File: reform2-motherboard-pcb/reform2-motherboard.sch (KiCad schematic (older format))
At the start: 44 parts, among them J15 Conn_01x33, J18 Conn_01x03_Male, J19 JTAG, J20 Conn_01x03_Male, SW3 SW_DIP_x01, SW5 SW_DIP_x04, SW6 SW_Push, U1 Nitrogen8M

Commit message: reform2-motherboard: schematics,PCB,BOM,models for R-2C (probably final)
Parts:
- H1, H2, H3: footprint MountingHole:MountingHole_3.2mm_M3_DIN965_Pad -> footprints:WA-SMSI-M2
- J19: footprint Connector_PinHeader_2.54mm:PinHeader_2x04_P2.54mm_Vertical -> Connector_PinHeader_1.27mm:PinHeader_2x05_P1.27mm_Vertical; symbol Connector:Conn_01x08_Male -> Connector:Conn_ARM_JTAG_SWD_10; Manufacturer_No 79425-408HLF -> 20021111-00010T4LF
- SW5: footprint Button_Switch_SMD:SW_DIP_SPSTx04_Slide_Omron_A6S-410x_W8.9mm_P2.54mm -> Button_Switch_SMD:SW_DIP_SPSTx04_Slide_Copal_CHS-04B_W7.62mm_P1.27mm; Manufacturer Omron -> Diptronics; Manufacturer_No A6S-4101-H -> DHA-04TQ
- SW6: footprint Button_Switch_SMD:SW_Push_1P1T_NO_CK_KMR2 -> footprints:UK-B0206-G3.8-250-JZ; Manufacturer C&K -> USAKRO; Manufacturer_No KMR221GLFS -> UK-B0206-G3.8-250-JZ
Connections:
- net ETH0_LED_LINK2: now also J19.10 (~RESET~); no longer J19.7 (Pin_7)
- net GND: now also J19.3 (GND), J19.9 (GNDDetect); no longer J19.8 (Pin_8)
- net IMX_JTAG_TDI: now also J19.8 (NC/TDI); no longer J19.2 (Pin_2)
- net IMX_JTAG_TMS: now also J19.2 (SWDIO/TMS); no longer J19.3 (Pin_3)
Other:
- moved on the sheet: R120
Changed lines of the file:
@@
 Sheet 1 9
 Title "MNT Reform 2"
-Date "2020-09-24"
-Rev "2.0R-1"
+Date "2020-10-29"
+Rev "2.0R-2C"
 Comp "MNT Research GmbH"
 Comment1 "https://mntre.com"
@@
 Text GLabel 6600 5350 0    50   Output ~ 0
 PCIE1_RESETn
-Text Notes 15250 4750 0    50   ~ 0
+Text Notes 14850 4400 0    50   ~ 0
 NOSTUFF
-Text Notes 14850 4750 0    50   ~ 0
-NOSTUFF
-Text Notes 15600 4750 0    50   ~ 0
+Text Notes 15550 4400 0    50   ~ 0
 NOSTUFF
 Wire Wire Line
@@
 	1    0    0    -1
 $EndComp
-Connection ~ 15650 5650
-Wire Wire Line
-	15650 5650 14800 5650
-Wire Wire Line
-	15650 5650 16050 5650
-Wire Wire Line
-	15950 5950 15950 5750
 $Comp
 L power:GND #PWR0219
 U 1 1 5F0CE58E
-P 15950 5950
-F 0 "#PWR0219" H 15950 5700 50  0001 C CNN
-F 1 "GND" H 15955 5777 50  0000 C CNN
-F 2 "" H 15950 5950 50  0001 C CNN
-F 3 "" H 15950 5950 50  0001 C CNN
-	1    15950 5950
-	1    0    0    -1
-$EndComp
-Wire Wire Line
-	15950 4450 15650 4450
-Connection ~ 15950 4450
-Wire Wire Line
-	15050 6050 15050 6000
+P 16750 6350
+F 0 "#PWR0219" H 16750 6100 50  0001 C CNN
+F 1 "GND" H 16755 6177 50  0000 C CNN
+F 2 "" H 16750 6350 50  0001 C CNN
+F 3 "" H 16750 6350 50  0001 C CNN
+	1    16750 6350
+	1    0    0    -1
+$EndComp
+Wire Wire Line
+	16750 4450 15650 4450
+Connection ~ 16750 4450
+Wire Wire Line
+	15950 6000 15950 5950
 $Comp
 L power:GND #PWR0218
 U 1 1 5F0856B7
-P 15050 6050
-F 0 "#PWR0218" H 15050 5800 50  0001 C CNN
-F 1 "GND" H 15055 5877 50  0000 C CNN
-F 2 "" H 15050 6050 50  0001 C CNN
-F 3 "" H 15050 6050 50  0001 C CNN
-	1    15050 6050
+P 15950 6000
+F 0 "#PWR0218" H 15950 5750 50  0001 C CNN
+F 1 "GND" H 15955 5827 50  0000 C CNN
+F 2 "" H 15950 6000 50  0001 C CNN
+F 3 "" H 15950 6000 50  0001 C CNN
+	1    15950 6000
 	1    0    0    -1
 $EndComp
@@
 Wire Wire Line
 	15650 4450 15650 4500
-Wire Wire Line
-	16300 4450 15950 4450
 $Comp
 L power:+3V3 #PWR0103
 U 1 1 5F0466BE
-P 16300 4450
-F 0 "#PWR0103" H 16300 4300 50  0001 C CNN
-F 1 "+3V3" H 16315 4623 50  0000 C CNN
-F 2 "" H 16300 4450 50  0001 C CNN
-F 3 "" H 16300 4450 50  0001 C CNN
-	1    16300 4450
-	1    0    0    -1
-$EndComp
-Wire Wire Line
-	16050 5550 14800 5550
-Wire Wire Line
-	15050 5350 16050 5350
-Connection ~ 15050 5350
-Wire Wire Line
-	15050 5800 15050 5350
-Wire Wire Line
-	14800 5350 15050 5350
-Connection ~ 15050 5250
-Wire Wire Line
-	15050 5250 16050 5250
-Wire Wire Line
-	15050 5250 14800 5250
-Wire Wire Line
-	15050 4700 15050 5250
-Connection ~ 15350 5150
-Wire Wire Line
-	15350 5150 16050 5150
-Wire Wire Line
-	15350 5150 14800 5150
-Wire Wire Line
-	15350 4700 15350 5150
-Text GLabel 14800 5150 0    50   Input ~ 0
+P 16750 4450
+F 0 "#PWR0103" H 16750 4300 50  0001 C CNN
+F 1 "+3V3" H 16765 4623 50  0000 C CNN
+F 2 "" H 16750 4450 50  0001 C CNN
+F 3 "" H 16750 4450 50  0001 C CNN
+	1    16750 4450
+	1    0    0    -1
+$EndComp
+Wire Wire Line
+	16250 5500 14800 5500
+Wire Wire Line
+	15950 5750 15950 5300
+Wire Wire Line
+	15350 5600 14800 5600
+Text GLabel 14800 5600 0    50   Input ~ 0
 IMX_JTAG_TDI
-Text GLabel 14800 5250 0    50   Output ~ 0
+Text GLabel 14800 5400 0    50   Output ~ 0
 IMX_JTAG_TMS
 Text GLabel 8700 8350 0    50   Output ~ 0
@@
 F 0 "H3" H 16400 8699 50  0000 L CNN
 F 1 "NGFF-Mount3" H 16400 8608 50  0000 L CNN
-F 2 "MountingHole:MountingHole_3.2mm_M3_DIN965_Pad" H 16300 8650 50  0001 C CNN
+F 2 "footprints:WA-SMSI-M2" H 16300 8650 50  0001 C CNN
 F 3 "~" H 16300 8650 50  0001 C CNN
 F 4 "y" H 16300 8650 50  0001 C CNN "Checked"
@@
 F 0 "H2" H 16400 7999 50  0000 L CNN
 F 1 "NGFF-Mount2" H 16400 7908 50  0000 L CNN
-F 2 "MountingHole:MountingHole_3.2mm_M3_DIN965_Pad" H 16300 7950 50  0001 C CNN
+F 2 "footprints:WA-SMSI-M2" H 16300 7950 50  0001 C CNN
 F 3 "~" H 16300 7950 50  0001 C CNN
 F 4 "y" H 16300 7950 50  0001 C CNN "Checked"
@@
 F 0 "H1" H 16400 7349 50  0000 L CNN
 F 1 "NGFF-Mount1" H 16400 7258 50  0000 L CNN
-F 2 "MountingHole:MountingHole_3.2mm_M3_DIN965_Pad" H 16300 7300 50  0001 C CNN
+F 2 "footprints:WA-SMSI-M2" H 16300 7300 50  0001 C CNN
 F 3 "~" H 16300 7300 50  0001 C CNN
 F 4 "y" H 16300 7300 50  0001 C CNN "Checked"
@@
 L Device:R_Small R120
 U 1 1 5E4B7E2C
-P 15050 5900
-F 0 "R120" H 15109 5946 50  0000 L CNN
-F 1 "100k" H 15109 5855 50  0000 L CNN
-F 2 "Resistor_SMD:R_0603_1608Metric" H 15050 5900 50  0001 C CNN
-F 3 "~" H 15050 5900 50  0001 C CNN
-F 4 "Vishay Dale" H 15050 5900 50  0001 C CNN "Manufacturer"
-F 5 "CRCW0603100KJNEAC" H 15050 5900 50  0001 C CNN "Manufacturer_No"
-F 6 "y" H 15050 5900 50  0001 C CNN "Checked"
-F 7 "Mouser" H 15050 5900 50  0001 C CNN "Distributor"
-	1    15050 5900
+P 15950 5850
+F 0 "R120" H 16009 5896 50  0000 L CNN
+F 1 "100k" H 16009 5805 50  0000 L CNN
+F 2 "Resistor_SMD:R_0603_1608Metric" H 15950 5850 50  0001 C CNN
+F 3 "~" H 15950 5850 50  0001 C CNN
+F 4 "Vishay Dale" H 15950 5850 50  0001 C CNN "Manufacturer"
+F 5 "CRCW0603100KJNEAC" H 15950 5850 50  0001 C CNN "Manufacturer_No"
+F 6 "y" H 15950 5850 50  0001 C CNN "Checked"
+F 7 "Mouser" H 15950 5850 50  0001 C CNN "Distributor"
+	1    15950 5850
 	1    0    0    -1
 $EndComp
@@
 Text GLabel 7400 7750 0    50   Output ~ 0
 IMX_JTAG_TDO
-Text GLabel 14800 5650 0    50   Output ~ 0
+Text GLabel 14800 5100 0    50   Output ~ 0
 IMX_JTAG_RSTn
-Text GLabel 14800 5350 0    50   Output ~ 0
+Text GLabel 14800 5300 0    50   Output ~ 0
 IMX_JTAG_TCK
-Text GLabel 14800 5550 0    50   Output ~ 0
+Text GLabel 14800 5500 0    50   Output ~ 0
 IMX_JTAG_TDO
 $Comp
@@
 	1    18500 3200
 	0    1    1    0
-$EndComp
-$Comp
-L Switch:SW_Push SW?
-U 1 1 5DBC8BEC
-P 18750 3200
-AR Path="/5CC81028/5DBC8BEC" Ref="SW?"  Part="1"
-AR Path="/5DBC8BEC" Ref="SW6"  Part="1"
-F 0 "SW6" H 18750 3485 50  0000 C CNN
-F 1 "SW_Push" H 18750 3394 50  0000 C CNN
-F 2 "Button_Switch_SMD:SW_Push_1P1T_NO_CK_KMR2" H 18750 3400 50  0001 C CNN
-F 3 "~" H 18750 3400 50  0001 C CNN
-F 4 "C&K" H 18750 3200 50  0001 C CNN "Manufacturer"
-F 5 "KMR221GLFS" H 18750 3200 50  0001 C CNN "Manufacturer_No"
-F 6 "y" H 18750 3200 50  0001 C CNN "Checked"
-F 7 "Mouser" H 18750 3200 50  0001 C CNN "Distributor"
-	1    18750 3200
-	1    0    0    -1
 $EndComp
 Text GLabel 7500 8550 0    50   Output ~ 0
@@
 Text GLabel 7300 10750 0    50   Input ~ 0
 IMX_WAKE
-Wire Wire Line
-	15650 4700 15650 5650
-$Comp
-L Connector:Conn_01x08_Male J19
+$Comp
+L Connector:Conn_ARM_JTAG_SWD_10 J19
 U 1 1 5ECAAFCE
-P 16250 5350
-F 0 "J19" H 16222 5324 50  0000 R CNN
-F 1 "JTAG" H 16222 5233 50  0000 R CNN
-F 2 "Connector_PinHeader_2.54mm:PinHeader_2x04_P2.54mm_Vertical" H 16250 5350 50  0001 C CNN
-F 3 "~" H 16250 5350 50  0001 C CNN
-F 4 "Amphenol FCI" H 16250 5350 50  0001 C CNN "Manufacturer"
-F 5 "79425-408HLF" H 16250 5350 50  0001 C CNN "Manufacturer_No"
-F 6 "y" H 16250 5350 50  0001 C CNN "Checked"
-F 7 "Mouser" H 16250 5350 50  0001 C CNN "Distributor"
-	1    16250 5350
+P 16750 5400
+F 0 "J19" H 16500 6100 50  0000 R CNN
+F 1 "JTAG" H 16550 6000 50  0000 R CNN
+F 2 "Connector_PinHeader_1.27mm:PinHeader_2x05_P1.27mm_Vertical" H 16750 5400 50  0001 C CNN
+F 3 "~" H 16750 5400 50  0001 C CNN
+F 4 "Amphenol FCI" H 16750 5400 50  0001 C CNN "Manufacturer"
+F 5 "20021111-00010T4LF" H 16750 5400 50  0001 C CNN "Manufacturer_No"
+F 6 "y" H 16750 5400 50  0001 C CNN "Checked"
+F 7 "Mouser" H 16750 5400 50  0001 C CNN "Distributor"
+	1    16750 5400
 	-1   0    0    -1
 $EndComp
-Wire Wire Line
-	16050 5750 15950 5750
-Wire Wire Line
-	16050 5050 15950 5050
-Wire Wire Line
-	15950 4450 15950 5050
-Wire Wire Line
-	15950 5750 15950 5450
-Wire Wire Line
-	15950 5450 16050 5450
-Connection ~ 15950 5750
 $Comp
 L power:+5V #PWR0104
@@
 F 0 "SW5" H 18950 6017 50  0000 C CNN
 F 1 "SW_DIP_x04" H 18950 5926 50  0000 C CNN
-F 2 "Button_Switch_SMD:SW_DIP_SPSTx04_Slide_Omron_A6S-410x_W8.9mm_P2.54mm" H 18950 5550 50  0001 C CNN
-F 3 "~" H 18950 5550 50  0001 C CNN
-F 4 "Omron" H 18950 5550 50  0001 C CNN "Manufacturer"
-F 5 "A6S-4101-H" H 18950 5550 50  0001 C CNN "Manufacturer_No"
+F 2 "Button_Switch_SMD:SW_DIP_SPSTx04_Slide_Copal_CHS-04B_W7.62mm_P1.27mm" H 18950 5550 50  0001 C CNN
+F 3 "" H 18950 5550 50  0001 C CNN
+F 4 "Diptronics" H 18950 5550 50  0001 C CNN "Manufacturer"
+F 5 "DHA-04TQ" H 18950 5550 50  0001 C CNN "Manufacturer_No"
 F 6 "y" H 18950 5550 50  0001 C CNN "Checked"
 F 7 "Mouser" H 18950 5550 50  0001 C CNN "Distributor"
@@
 	1    0    0    -1
 $EndComp
+$Comp
+L Switch:SW_Push SW?
+U 1 1 5DBC8BEC
+P 18750 3200
+AR Path="/5CC81028/5DBC8BEC" Ref="SW?"  Part="1"
+AR Path="/5DBC8BEC" Ref="SW6"  Part="1"
+F 0 "SW6" H 18750 3485 50  0000 C CNN
+F 1 "SW_Push" H 18750 3394 50  0000 C CNN
+F 2 "footprints:UK-B0206-G3.8-250-JZ" H 18750 3400 50  0001 C CNN
+F 3 "~" H 18750 3400 50  0001 C CNN
+F 4 "USAKRO" H 18750 3200 50  0001 C CNN "Manufacturer"
+F 5 "UK-B0206-G3.8-250-JZ" H 18750 3200 50  0001 C CNN "Manufacturer_No"
+F 6 "y" H 18750 3200 50  0001 C CNN "Checked"
+F 7 "Mouser" H 18750 3200 50  0001 C CNN "Distributor"
+	1    18750 3200
+	1    0    0    -1
+$EndComp
+Wire Wire Line
+	14800 5400 15050 5400
+Wire Wire Line
+	14800 5100 15650 5100
+Text Notes 15200 4400 0    50   ~ 0
+NOSTUFF
+Wire Wire Line
+	15050 5400 15050 4700
+Connection ~ 15050 5400
+Wire Wire Line
+	15050 5400 16250 5400
+Wire Wire Line
+	15350 4700 15350 5600
+Wire Wire Line
+	15350 5600 16250 5600
+Connection ~ 15350 5600
+Connection ~ 15950 5300
+Wire Wire Line
+	15950 5300 16250 5300
+Wire Wire Line
+	14800 5300 15950 5300
+Wire Wire Line
+	15650 4700 15650 5100
+Connection ~ 15650 5100
+Wire Wire Line
+	15650 5100 16250 5100
+Wire Wire Line
+	16750 4450 16750 4800
+Wire Wire Line
+	16750 6100 16850 6100
+Wire Wire Line
+	16850 6100 16850 6000
+Wire Wire Line
+	16750 6000 16750 6100
+Connection ~ 16750 6100
+Wire Wire Line
+	16750 6100 16750 6350
 $EndSCHEMATC

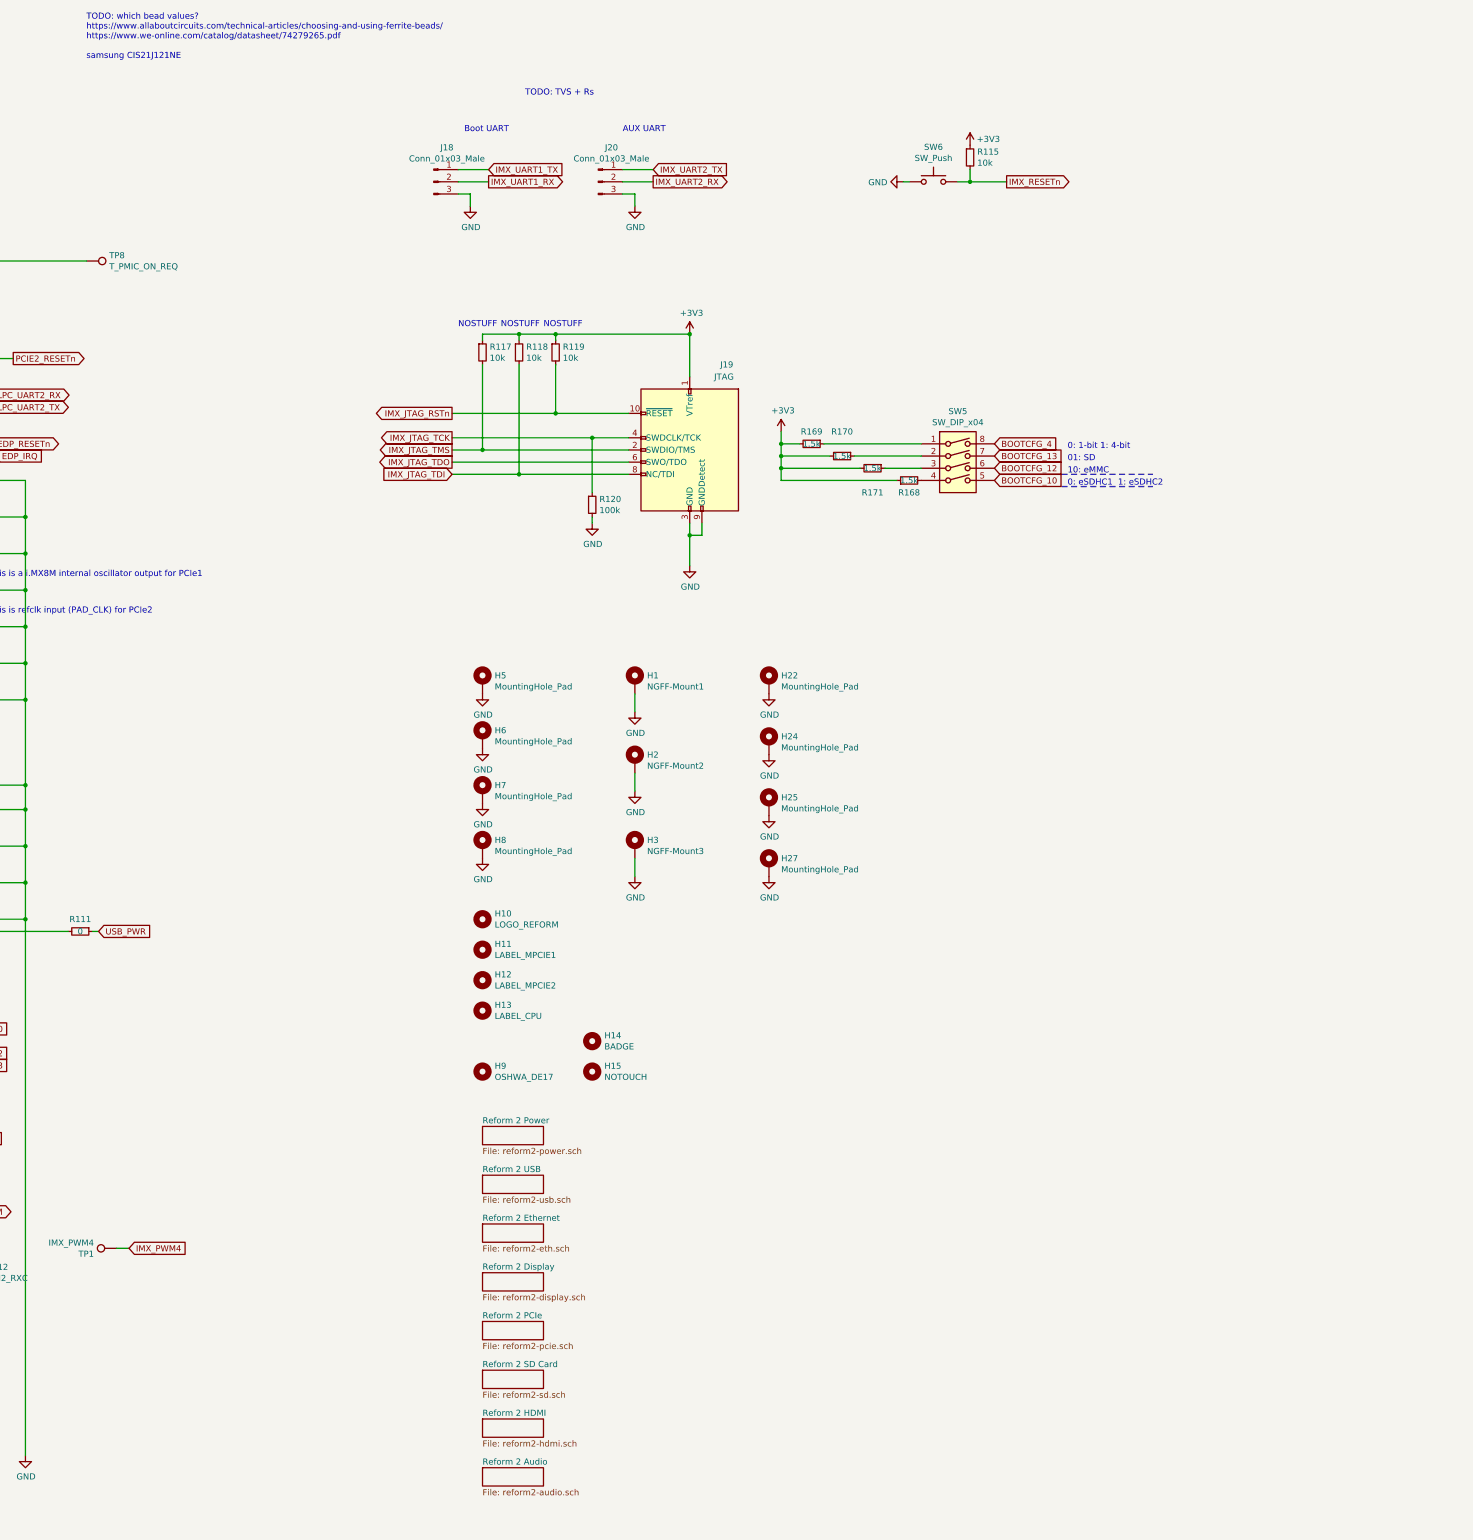
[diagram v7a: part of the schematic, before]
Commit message: reform2-motherboard: add pdf schematics
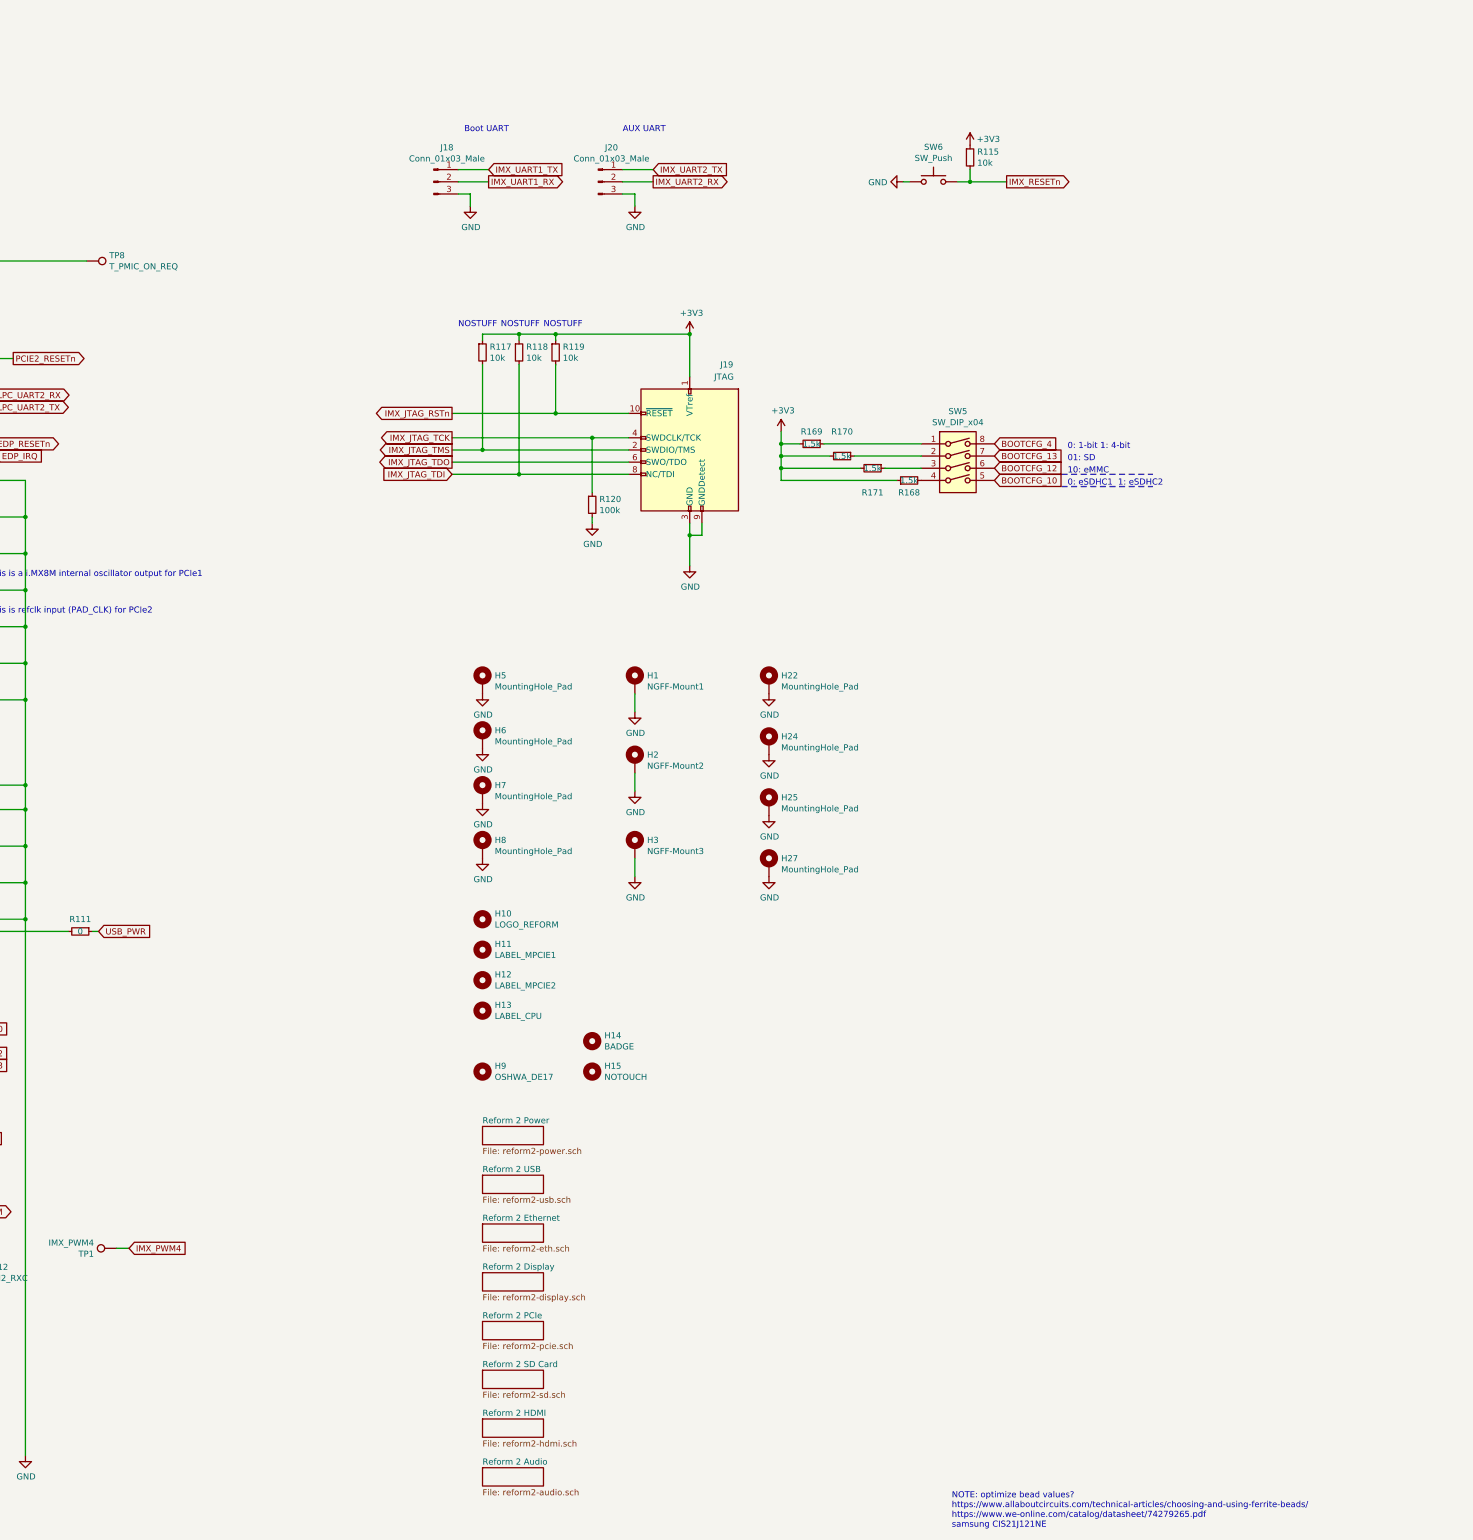
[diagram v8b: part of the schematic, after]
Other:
- note added: "NOTE: optimize bead values?\nhttps://www.allaboutcircuits.com/technical-articles/choosing-and-using-ferrite-beads/\nhttps://www.we-online.com/catalog/datasheet/74279265.pdf\nsamsung CIS21J121NE"
- note removed: "TODO: TVS + Rs"
- note removed: "TODO: which bead values?\nhttps://www.allaboutcircuits.com/technical-articles/choosing-and-using-ferrite-beads/\nhttps://www.we-online.com/catalog/datasheet/74279265.pdf\n\nsamsung CIS21J121NE"
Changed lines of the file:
@@
 Wire Wire Line
 	10400 5450 11050 5450
-Text Notes 11800 2200 0    50   ~ 0
-TODO: which bead values?\nhttps://www.allaboutcircuits.com/technical-articles/choosing-and-using-ferrite-beads/\nhttps://www.we-online.com/catalog/datasheet/74279265.pdf\n\nsamsung CIS21J121NE
-Text Notes 15400 2500 0    50   ~ 0
-TODO: TVS + Rs
+Text Notes 18900 14250 0    50   ~ 0
+NOTE: optimize bead values?\nhttps://www.allaboutcircuits.com/technical-articles/choosing-and-using-ferrite-beads/\nhttps://www.we-online.com/catalog/datasheet/74279265.pdf\nsamsung CIS21J121NE
 $Comp
 L Mechanical:MountingHole H14
